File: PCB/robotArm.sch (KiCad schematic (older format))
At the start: 66 parts, among them J1 Motor_eje_X, J10 Gripper, J11 Conector Auxiliar 2, J12 5v, J13 End-Stop-X, J14 End-Stop-Y, J15 End-Stop-Z, J16 jumperLed5v, J17 Conector Auxiliar 1, J18 jumperLedVbat, J19 Vbat, J2 3.3v, J3 Motor_eje_Y, J4 Motor_eje_Z, J5 micro pasos X, J6 micro pasos Y, J7 micro pasos Z, J8 Conector I2C, J9 jumperLed3.3v, Q1 BC548, Q2 BC548, Q3 BC548, SW1 SW_Push, U1 YAAJ_BluePill

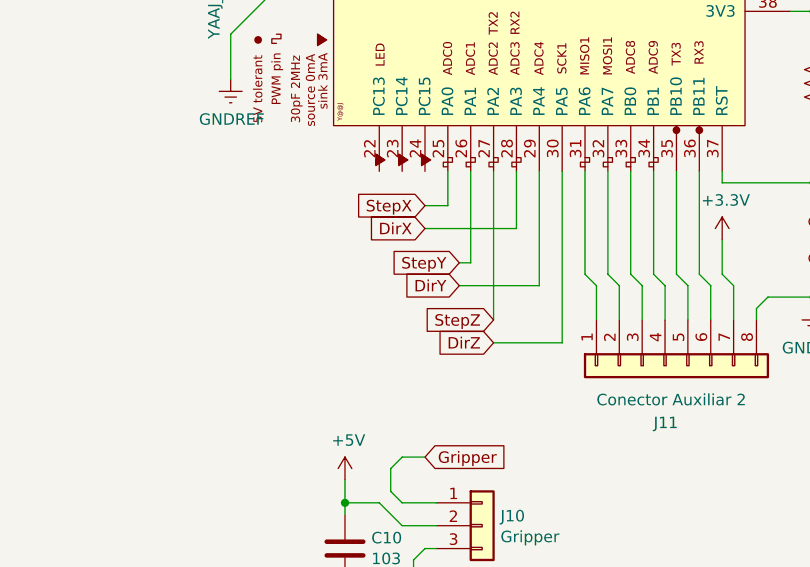
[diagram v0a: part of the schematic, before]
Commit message: se agregó gitignore al proyecto
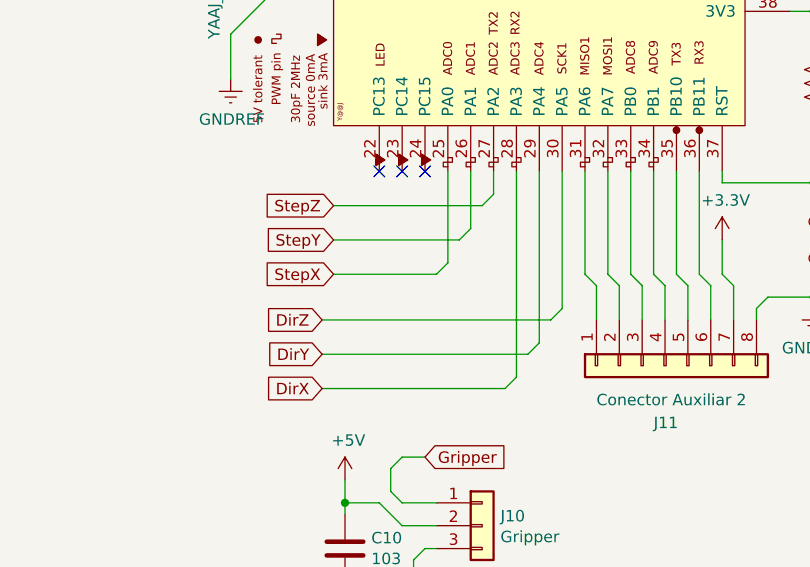
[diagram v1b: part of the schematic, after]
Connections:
- no-connect marks 0 -> 3
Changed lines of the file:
@@
 encoding utf-8
 Sheet 1 1
-Title ""
-Date ""
-Rev ""
-Comp ""
-Comment1 ""
-Comment2 ""
-Comment3 ""
-Comment4 ""
+Title "Placa de control para brazo robótico de 3 GDL."
+Date "2023-06-19"
+Rev "0.3.4"
+Comp "Universidad Nacional de Cuyo (UNCuyo)"
+Comment1 "Fines de carrera opticos normalmente cerrados (NC)"
+Comment2 "Revisar configuración del STM32cubeIDE"
+Comment3 "Legajo: 11807  estudiante de ingeniería en Mecatrónica"
+Comment4 "Alumno: Mario Stefano Papetti Funes"
 $EndDescr
 $Comp
@@
 Wire Wire Line
 	2300 6450 3250 6450
-Text GLabel 6250 5800 0    50   Input ~ 0
+Text GLabel 5700 5700 0    50   Input ~ 0
 StepY
-Text GLabel 6250 5900 0    50   Input ~ 0
+Text GLabel 5650 6200 0    50   Input ~ 0
 DirY
-Text GLabel 6400 6050 0    50   Input ~ 0
-StepZ
-Text GLabel 6400 6150 0    50   Input ~ 0
+Text GLabel 5650 6050 0    50   Input ~ 0
 DirZ
-Text GLabel 6100 5650 0    50   Input ~ 0
+Text GLabel 5650 6350 0    50   Input ~ 0
 DirX
 $Comp
@@
 Text GLabel 6100 6650 2    50   Input ~ 0
 Gripper
-Text GLabel 6100 5550 0    50   Input ~ 0
-StepX
-Wire Wire Line
-	6700 5400 6700 6150
-Wire Wire Line
-	6700 6150 6400 6150
-Wire Wire Line
-	6250 5900 6600 5900
-Wire Wire Line
-	6600 5900 6600 5400
-Wire Wire Line
-	6500 5400 6500 5650
-Wire Wire Line
-	6500 5650 6100 5650
-Wire Wire Line
-	6100 5550 6200 5550
-Wire Wire Line
-	6200 5550 6200 5400
-Wire Wire Line
-	6250 5800 6300 5800
-Wire Wire Line
-	6300 5800 6300 5400
-Wire Wire Line
-	6400 5400 6400 6050
 Text GLabel 5700 3600 0    50   Input ~ 0
 Gripper
@@
 Wire Wire Line
 	6000 6650 6100 6650
+NoConn ~ 5900 5400
+NoConn ~ 6000 5400
+NoConn ~ 6100 5400
+Text GLabel 5700 5850 0    50   Input ~ 0
+StepX
+Text GLabel 5700 5550 0    50   Input ~ 0
+StepZ
+Wire Wire Line
+	5700 5550 6350 5550
+Wire Wire Line
+	6350 5550 6400 5500
+Wire Wire Line
+	6400 5500 6400 5400
+Wire Wire Line
+	5700 5700 6250 5700
+Wire Wire Line
+	6250 5700 6300 5650
+Wire Wire Line
+	6300 5650 6300 5400
+Wire Wire Line
+	6200 5400 6200 5800
+Wire Wire Line
+	6200 5800 6150 5850
+Wire Wire Line
+	6150 5850 5700 5850
+Wire Wire Line
+	6650 6050 6700 6000
+Wire Wire Line
+	5650 6050 6650 6050
+Wire Wire Line
+	6700 5400 6700 6000
+Wire Wire Line
+	6600 6150 6550 6200
+Wire Wire Line
+	5650 6200 6550 6200
+Wire Wire Line
+	6600 5400 6600 6150
+Wire Wire Line
+	6500 6300 6450 6350
+Wire Wire Line
+	6500 5400 6500 6300
+Wire Wire Line
+	5650 6350 6450 6350
 $EndSCHEMATC

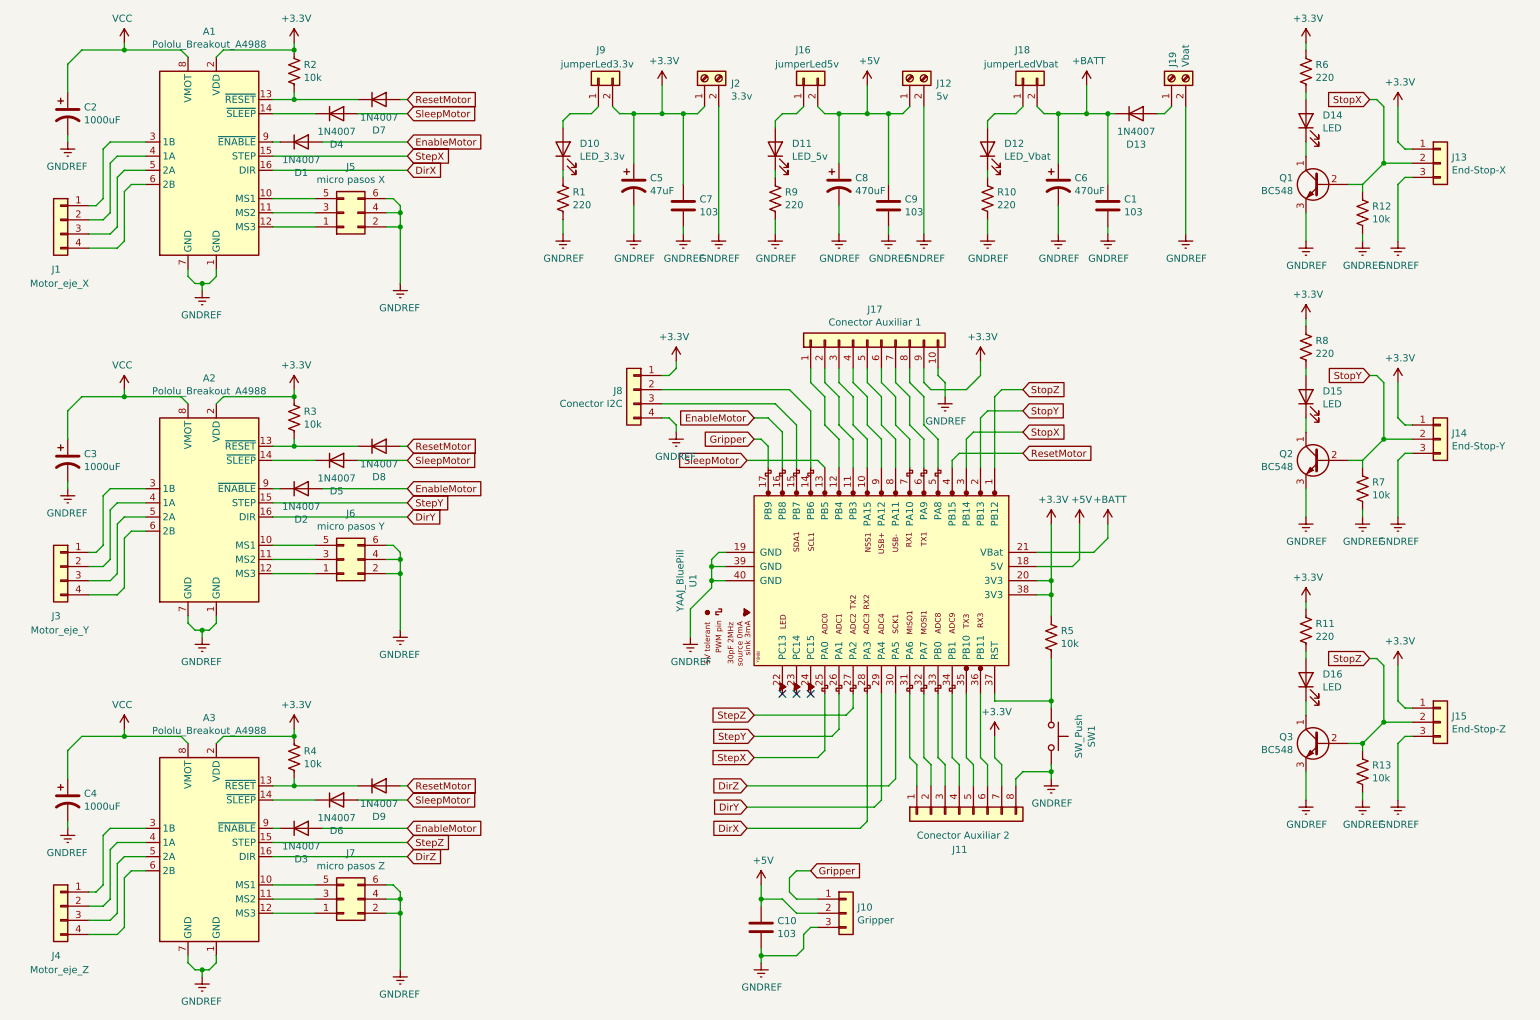
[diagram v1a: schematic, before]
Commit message: Se avanzó con el diseño de la PCB, falta resolver Vin
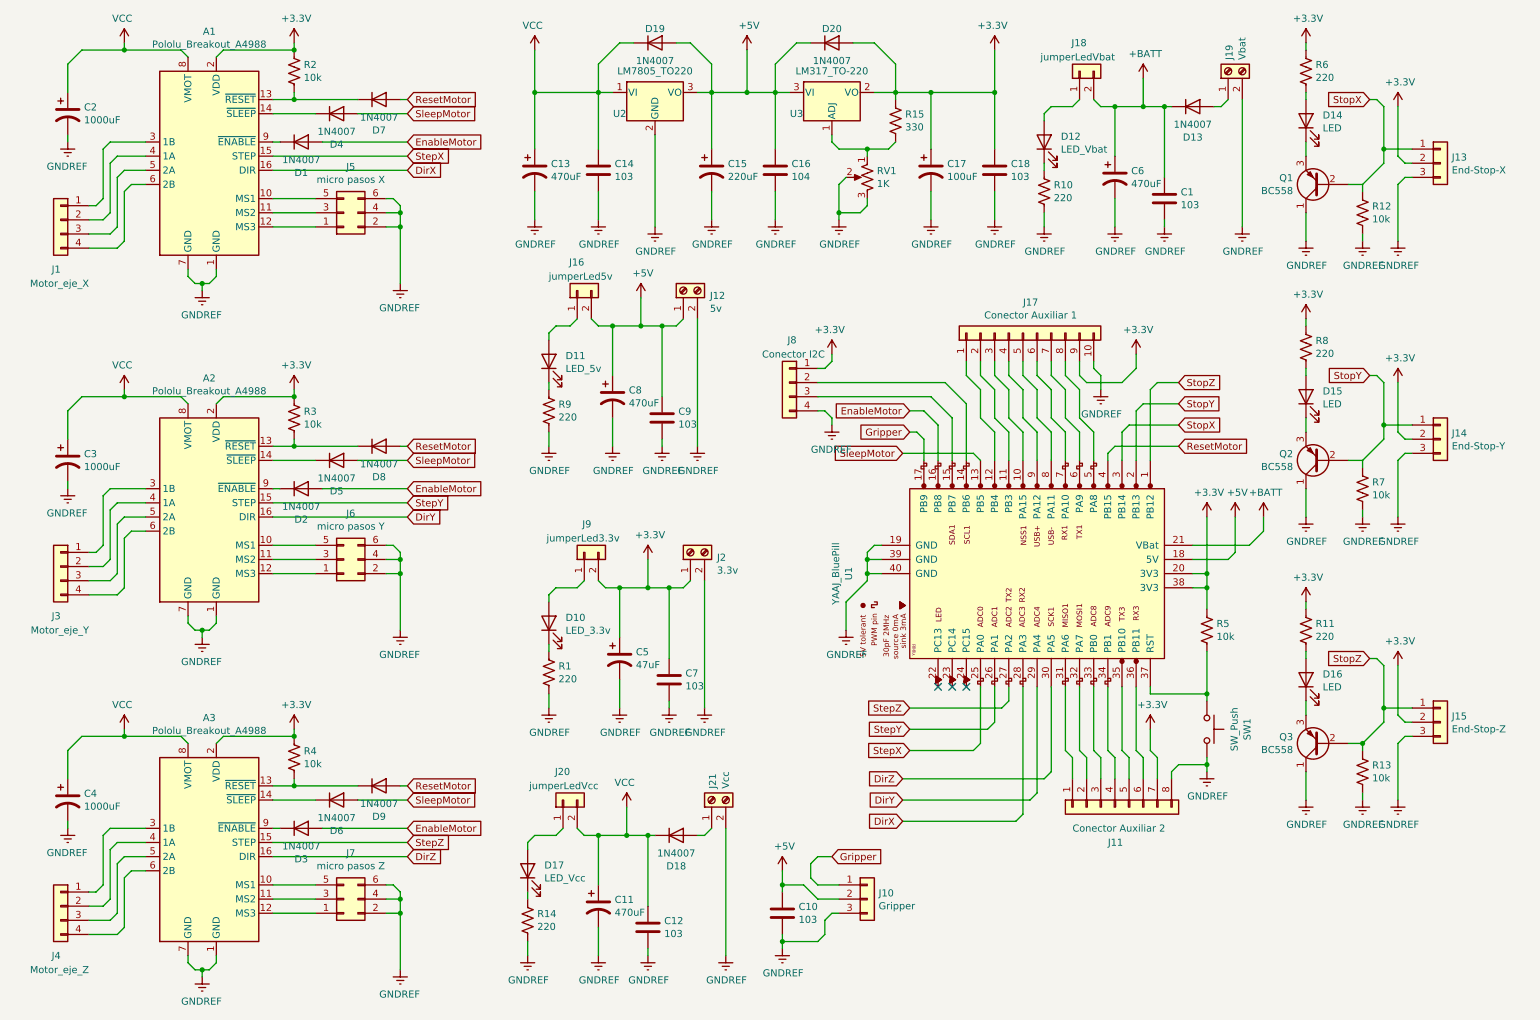
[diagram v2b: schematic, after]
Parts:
- removed Q1, Q2, Q3: BC548, Package_TO_SOT_THT:TO-92_HandSolder, symbol Transistor_BJT:BC548
- added C11, C13: 470uF, Capacitor_THT:CP_Radial_D8.0mm_P3.80mm, symbol Device:CP1
- added C12, C14, C18: 103, Capacitor_THT:C_Disc_D8.0mm_W2.5mm_P5.00mm, symbol Device:C
- added C15: 220uF, Capacitor_THT:CP_Radial_D8.0mm_P3.80mm, symbol Device:CP1
- added C16: 104, Capacitor_THT:C_Disc_D8.0mm_W2.5mm_P5.00mm, symbol Device:C
- added C17: 100uF, Capacitor_THT:CP_Radial_D8.0mm_P3.80mm, symbol Device:CP1
- added D17: LED_Vcc, LED_THT:LED_D5.0mm, symbol Device:LED
- added D18, D19, D20: 1N4007, Diode_THT:D_DO-41_SOD81_P10.16mm_Horizontal, symbol Diode:1N4007
- added J20: jumperLedVcc, Connector_PinHeader_2.54mm:PinHeader_2x01_P2.54mm_Vertical, symbol Connector_Generic:Conn_01x02
- added J21: Vcc, TerminalBlock:TerminalBlock_bornier-2_P5.08mm, symbol Connector:Screw_Terminal_01x02
- added Q1, Q2, Q3: BC558, Package_TO_SOT_THT:TO-92_HandSolder, symbol Transistor_BJT:BC558
- added R14: 220, Resistor_THT:R_Axial_DIN0207_L6.3mm_D2.5mm_P10.16mm_Horizontal, symbol Device:R_US
- added R15: 330, Resistor_THT:R_Axial_DIN0207_L6.3mm_D2.5mm_P10.16mm_Horizontal, symbol Device:R_US
- added RV1: 1K, Potentiometer_THT:Potentiometer_Bourns_3266W_Vertical, symbol Device:R_POT_US
- added U2: LM7805_TO220, Package_TO_SOT_THT:TO-220-3_Vertical, symbol Regulator_Linear:LM7805_TO220
- added U3: LM317_TO-220, Package_TO_SOT_THT:TO-220-3_Vertical, symbol Regulator_Linear:LM317_TO-220
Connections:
- net +3V3: now also J13.2 (Pin_2), J14.2 (Pin_2), J15.2 (Pin_2), C17.1, C18.1, D20.2 (A), R15.1, U3.2 (VO); no longer J13.1 (Pin_1), J14.1 (Pin_1), J15.1 (Pin_1)
- net +5V: now also C15.1, C16.1, D19.2 (A), D20.1 (K), U2.3 (VO), U3.3 (VI)
- net GNDREF: now also C11.2, C12.2, C13.2, C14.2, C15.2, C16.2, C17.2, C18.2, J21.2 (Pin_2), Q1.1 (C), Q2.1 (C), Q3.1 (C), R14.2, RV1.2, RV1.3, U2.2 (GND)
- net StopX: now also J13.1 (Pin_1), Q1.2 (B); no longer J13.2 (Pin_2)
- net StopY: now also J14.1 (Pin_1), Q2.2 (B); no longer J14.2 (Pin_2)
- net StopZ: now also J15.1 (Pin_1), Q3.2 (B); no longer J15.2 (Pin_2)
- net VCC: now also C11.1, C12.1, C13.1, C14.1, D18.1 (K), D19.1 (K), J20.2 (Pin_2), U2.1 (VI)
- net at D15.1 (K): now also Q2.3 (E)
- net at D14.1 (K): now also Q1.3 (E)
- net at D16.1 (K): now also Q3.3 (E)
- new net: D17.1 (K), R14.1
- new net: D17.2 (A), J20.1 (Pin_1)
- new net: D18.2 (A), J21.1 (Pin_1)
- new net: R15.2, RV1.1, U3.1 (ADJ)
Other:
- moved on the sheet: C1, C10, C5, C6, C7, C8, C9, D10, D11, D12, D13, J10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

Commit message: Se avanzó con el diseño de la PCB
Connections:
- net +3V3: now also J17.1 (Pin_1); no longer J17.9 (Pin_9)
- net at U1.10 (PA15): now also J17.4 (Pin_4); no longer J17.3 (Pin_3)
- net at U1.11 (PB3): now also J17.3 (Pin_3); no longer J17.2 (Pin_2)
- net at U1.12 (PB4): now also J17.2 (Pin_2); no longer J17.1 (Pin_1)
- net at U1.5 (PA8): now also J17.9 (Pin_9); no longer J17.8 (Pin_8)
- net at U1.6 (PA9): now also J17.8 (Pin_8); no longer J17.7 (Pin_7)
- net at U1.7 (PA10): now also J17.7 (Pin_7); no longer J17.6 (Pin_6)
- net at U1.8 (PA11): now also J17.6 (Pin_6); no longer J17.5 (Pin_5)
- net at U1.9 (PA12): now also J17.5 (Pin_5); no longer J17.4 (Pin_4)
- no-connect marks 3 -> 4
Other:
- moved on the sheet: J17

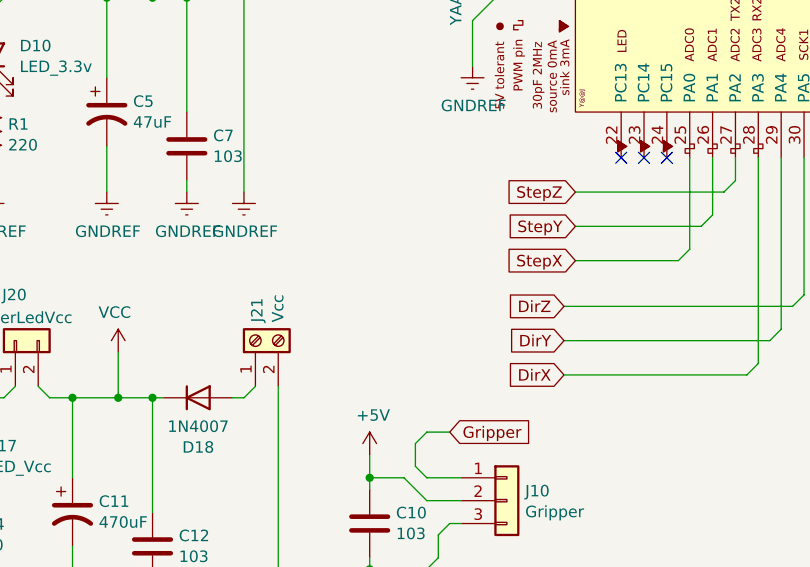
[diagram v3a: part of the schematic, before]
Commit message: Se logró conectar todos lso dispositivos en la PCB
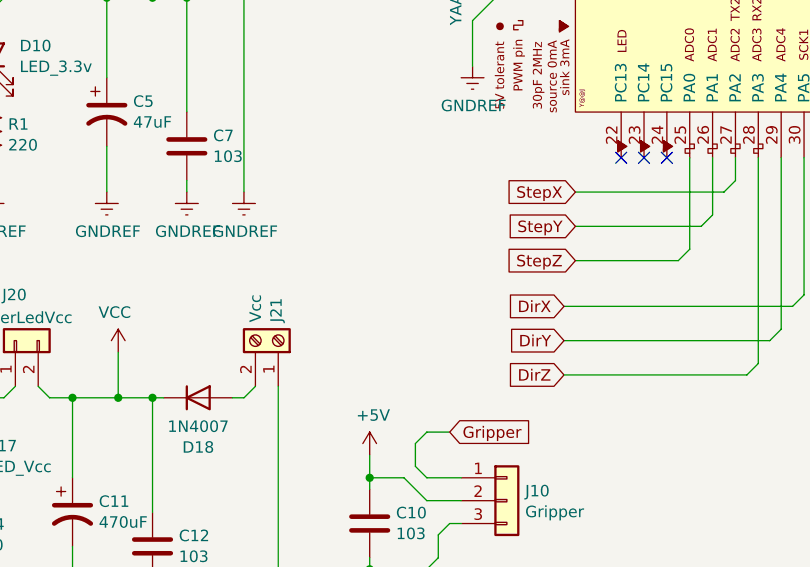
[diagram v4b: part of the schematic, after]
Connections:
- net DirX: now also U1.30 (PA5); no longer U1.28 (PA3)
- net DirZ: now also U1.28 (PA3); no longer U1.30 (PA5)
- net GNDREF: now also J21.1 (Pin_1); no longer J21.2 (Pin_2)
- net StepX: now also U1.27 (PA2); no longer U1.25 (PA0)
- net StepZ: now also U1.25 (PA0); no longer U1.27 (PA2)
- net at D18.2 (A): now also J21.2 (Pin_2); no longer J21.1 (Pin_1)

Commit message: Se agregó LCD i2c y lógica de CDC
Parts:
- R12, R13, R7: value 10k -> 47k
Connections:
- net +3V3: now also J17.2 (Pin_2), R12.2, R13.2, R7.2
- net GNDREF: now also J17.9 (Pin_9); no longer R12.2, R13.2, R7.2
- net SleepMotor: now also U1.12 (PB4); no longer U1.13 (PB5)
- net StepY: now also U1.5 (PA8); no longer U1.26 (PA1)
- net StopX: now also R7.1; no longer R12.1
- net StopY: now also R12.1; no longer R7.1
- no-connect marks 4 -> 6
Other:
- moved on the sheet: R13

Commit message: update interface
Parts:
- removed C1: 103, Capacitor_THT:C_Disc_D8.0mm_W2.5mm_P5.00mm, symbol Device:C
- removed C6: 470uF, Capacitor_THT:CP_Radial_D8.0mm_P3.80mm, symbol Device:CP1
- removed D1, D13, D2, D3, D4, D5, D6, D7, D8, D9: 1N4007, Diode_THT:D_DO-41_SOD81_P10.16mm_Horizontal, symbol Diode:1N4007
- removed D12: LED_Vbat, LED_THT:LED_D5.0mm, symbol Device:LED
- removed J19: Vbat, TerminalBlock:TerminalBlock_bornier-2_P5.08mm, symbol Connector:Screw_Terminal_01x02
- removed R10: 220, Resistor_THT:R_Axial_DIN0207_L6.3mm_D2.5mm_P10.16mm_Horizontal, symbol Device:R_US
- added C19, C20: 103, Capacitor_THT:C_Disc_D8.0mm_W2.5mm_P5.00mm, symbol Device:C
- added D1: LED_Home, LED_THT:LED_D5.0mm, symbol Device:LED
- added D2: LED_Wait, LED_THT:LED_D5.0mm, symbol Device:LED
- added D3: LED_Finish, LED_THT:LED_D5.0mm, symbol Device:LED
- added R16, R17, R18: 1k, Resistor_THT:R_Axial_DIN0207_L6.3mm_D2.5mm_P10.16mm_Horizontal, symbol Device:R_US
- added R19: 10k, Resistor_THT:R_Axial_DIN0207_L6.3mm_D2.5mm_P10.16mm_Horizontal, symbol Device:R_US
- added SW2: STOP_EM, Button_Switch_THT:SW_PUSH_6mm_H5mm, symbol Switch:SW_Push
- C11, C8: value 470uF -> 10uF
- C5: value 47uF -> 10uF
- J18: value jumperLedVbat -> Pulsador Externo; footprint Connector_PinHeader_2.54mm:PinHeader_2x01_P2.54mm_Vertical -> Connector_PinHeader_2.54mm:PinHeader_1x02_P2.54mm_Vertical
- J5, J6, J7: footprint Connector_PinSocket_2.54mm:PinSocket_2x03_P2.54mm_Vertical -> Connector_PinHeader_2.54mm:PinHeader_2x03_P2.54mm_Vertical
- R2, R3, R4: value 10k -> 4.7k
- SW1: value SW_Push -> RESET
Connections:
- net +3V3: now also J5.2 (Pin_2), J5.4 (Pin_4), J5.6 (Pin_6), J6.2 (Pin_2), J6.4 (Pin_4), J6.6 (Pin_6), J7.2 (Pin_2), J7.4 (Pin_4), J7.6 (Pin_6), R19.1
- net EnableMotor: now also A1.9 (~ENABLE), A2.9 (~ENABLE), A3.9 (~ENABLE)
- net GNDREF: now also J18.1 (Pin_1), C19.2, C20.2, D1.1 (K), D2.1 (K), D3.1 (K), SW2.2; no longer J5.2 (Pin_2), J5.4 (Pin_4), J5.6 (Pin_6), J6.2 (Pin_2), J6.4 (Pin_4), J6.6 (Pin_6), J7.2 (Pin_2), J7.4 (Pin_4), J7.6 (Pin_6)
- net StepY: now also U1.26 (PA1); no longer U1.5 (PA8)
- net at U1.10 (PA15): now also J17.3 (Pin_3); no longer J17.4 (Pin_4)
- net home: now reaches U1.11 (PB3)
- net home: now also R16.1; no longer J17.3 (Pin_3)
- net wait: now reaches U1.13 (PB5)
- net wait: now also R18.1
- net at R5.2, SW1.1, U1.37 (RST): now also C20.1
- net at J17.8 (Pin_8): now also U1.5 (PA8); no longer U1.6 (PA9)
- net at J17.7 (Pin_7): now also U1.6 (PA9); no longer U1.7 (PA10)
- net at J17.6 (Pin_6): now also U1.7 (PA10); no longer U1.8 (PA11)
- net at J17.5 (Pin_5): now also U1.8 (PA11); no longer U1.9 (PA12)
- net at A3.10 (MS1): now also J7.1 (Pin_1); no longer J7.5 (Pin_5)
- net at A3.12 (MS3): now also J7.5 (Pin_5); no longer J7.1 (Pin_1)
- net at A3.13 (~RESET), R4.2: now also A3.14 (~SLEEP)
- net at A2.10 (MS1): now also J6.1 (Pin_1); no longer J6.5 (Pin_5)
- net at A2.12 (MS3): now also J6.5 (Pin_5); no longer J6.1 (Pin_1)
- net at A2.13 (~RESET), R3.2: now also A2.14 (~SLEEP)
- net at A1.10 (MS1): now also J5.1 (Pin_1); no longer J5.5 (Pin_5)
- net at A1.12 (MS3): now also J5.5 (Pin_5); no longer J5.1 (Pin_1)
- net at A1.13 (~RESET), R2.2: now also A1.14 (~SLEEP)
- net +BATT: no longer names the net of U1.21 (VBat)
- net +BATT: no longer J18.2 (Pin_2)
- net ResetMotor renamed STOP
- net STOP: now also J18.2 (Pin_2), C19.1, R19.2, SW2.1
- net SleepMotor renamed finish
- net finish: now also R17.1
- new net: J17.4 (Pin_4), U1.9 (PA12)
- new net: D1.2 (A), R16.2
- new net: D3.2 (A), R17.2
- new net: D2.2 (A), R18.2
- no-connect marks 6 -> 5
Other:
- moved on the sheet: C10, C11, C12, C13, C14, C15, C16, C17, C18, C5, C7, C8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
